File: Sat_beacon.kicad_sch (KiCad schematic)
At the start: 123 parts, among them IC1 LMX2581ESQE_NOPB, IC2 LMX2581ESQE_NOPB, J1 Conn_01x05_Pin, J2 Conn_01x05_Pin, J3 Conn_01x03_Pin, J4 MMCX, J5 MMCX, Q1 BC817-40, Q2 BC817-40, Q3 BC817-40, Q4 BC817-40, SW1 SW_SPDT_312, SW2 SW_Omron_B3FS, SW3 SW_Omron_B3FS, SW4 SW_Omron_B3FS, SW5 SW_Omron_B3FS, U1 STM32C011F6Px, U2 LD1117V33, U3 MCP1700x-330xxMB, U4 1720BL15B0050002E, U5 1720BL15B0050002E, Y1 FT2MHUPM10.0-T1

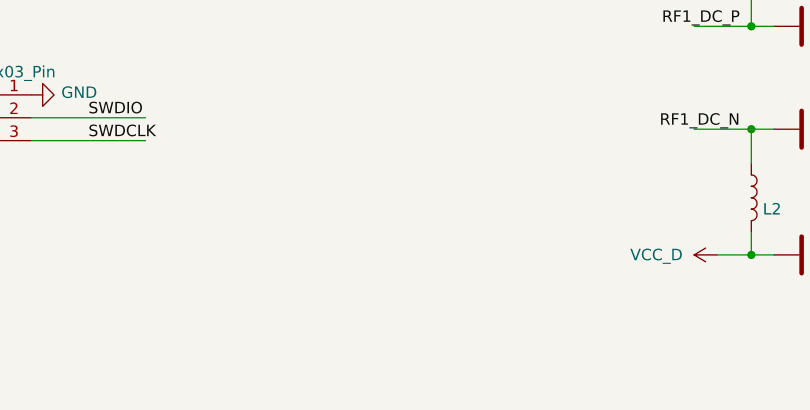
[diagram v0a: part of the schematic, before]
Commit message: RF C added, replacement needed
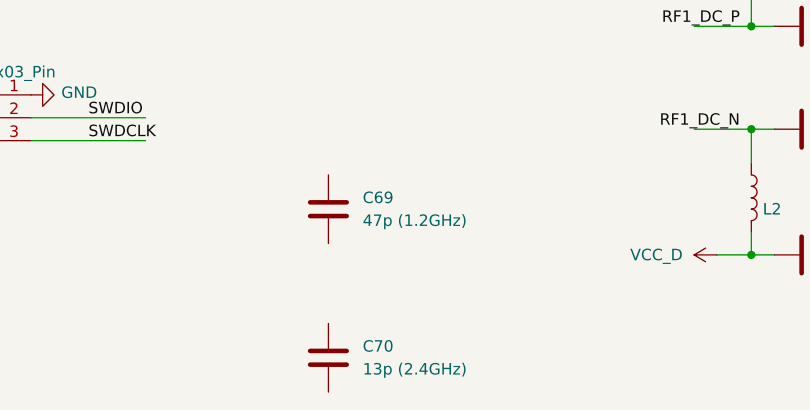
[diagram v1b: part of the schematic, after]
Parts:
- added C69: 47p (1.2GHz), Capacitor_SMD:C_0402_1005Metric, symbol Device:C
- added C70: 13p (2.4GHz), Capacitor_SMD:C_0402_1005Metric, symbol Device:C
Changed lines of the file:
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@@
+	)
+	(symbol
+		(lib_id "Device:C")
+		(at 123.19 215.9 0)
+		(unit 1)
+		(exclude_from_sim no)
+		(in_bom yes)
+		(on_board yes)
+		(dnp no)
+		(fields_autoplaced yes)
+		(property "Reference" "C70"
+			(at 127 214.6299 0)
+			(effects
+				(font
+					(size 1.27 1.27)
+				)
+				(justify left)
+			)
+		)
+		(property "Value" "13p (2.4GHz)"
+			(at 127 217.1699 0)
+			(effects
+				(font
+					(size 1.27 1.27)
+				)
+				(justify left)
+			)
+		)
+		(property "Footprint" "Capacitor_SMD:C_0402_1005Metric"
+			(at 124.1552 219.71 0)
+			(effects
+				(font
+					(size 1.27 1.27)
+				)
+				(hide yes)
+			)
+		)
+		(property "Datasheet" "https://www.tme.eu/cz/details/gjm1555c1h130gb01d/kondenzatory-mlcc-smd/murata/"
+			(at 123.19 215.9 0)
+			(effects
+				(font
+					(size 1.27 1.27)
+				)
+				(hide yes)
+			)
+		)
+		(property "Description" "Unpolarized capacitor"
+			(at 123.19 215.9 0)
+			(effects
+				(font
+					(size 1.27 1.27)
+				)
+				(hide yes)
+			)
+		)
+		(pin "2"
+		)
+		(pin "1"
+		)
+		(instances
+			(project "Sat_beacon"
+				(path "/d50b57a8-fbd1-4b9f-a519-640b54fbccac"
+					(reference "C70")
+					(unit 1)
+				)
+			)
+		)
 	)
 	(symbol
@@
 					(unit 1)
 				)
+			)
+		)
+	)
+	(symbol
+		(lib_id "Device:C")
+		(at 123.19 199.39 0)
+		(unit 1)
+		(exclude_from_sim no)
+		(in_bom yes)
+		(on_board yes)
+		(dnp no)
+		(fields_autoplaced yes)
+		(property "Reference" "C69"
+			(at 127 198.1199 0)
+			(effects
+				(font
+					(size 1.27 1.27)
+				)
+				(justify left)
+			)
+		)
+		(property "Value" "47p (1.2GHz)"
+			(at 127 200.6599 0)
+			(effects
+				(font
+					(size 1.27 1.27)
+				)
+				(justify left)
+			)
+		)
+		(property "Footprint" "Capacitor_SMD:C_0402_1005Metric"
+			(at 124.1552 203.2 0)
+			(effects
+				(font
+					(size 1.27 1.27)
+				)
+				(hide yes)
+			)
+		)
+		(property "Datasheet" "https://www.tme.eu/cz/details/gjm1555c1h470jb01d/kondenzatory-mlcc-smd/murata/"
+			(at 123.19 199.39 0)
+			(effects
+				(font
+					(size 1.27 1.27)
+				)
+				(hide yes)
+			)
+		)
+		(property "Description" "Unpolarized capacitor"
+			(at 123.19 199.39 0)
+			(effects
+				(font
+					(size 1.27 1.27)
+				)
+				(hide yes)
+			)
+		)
+		(pin "2"
+		)
+		(pin "1"
+		)
+		(instances
+			(project ""
+				(path "/d50b57a8-fbd1-4b9f-a519-640b54fbccac"
+					(reference "C69")
+					(unit 1)
+				)

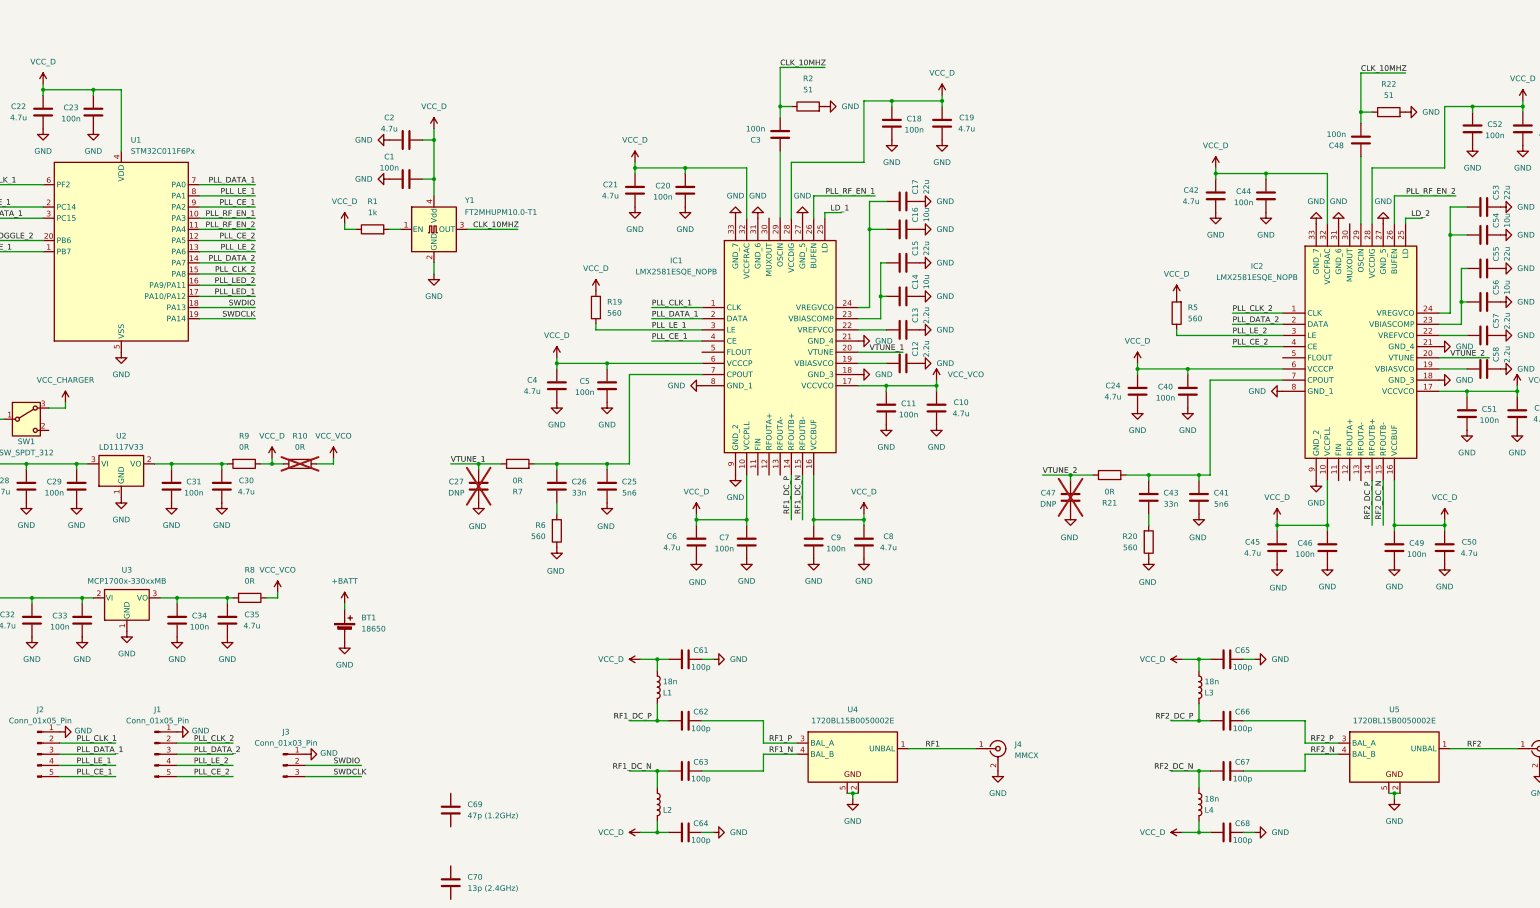
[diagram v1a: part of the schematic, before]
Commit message: footprint fixes, BOM and CSV generated
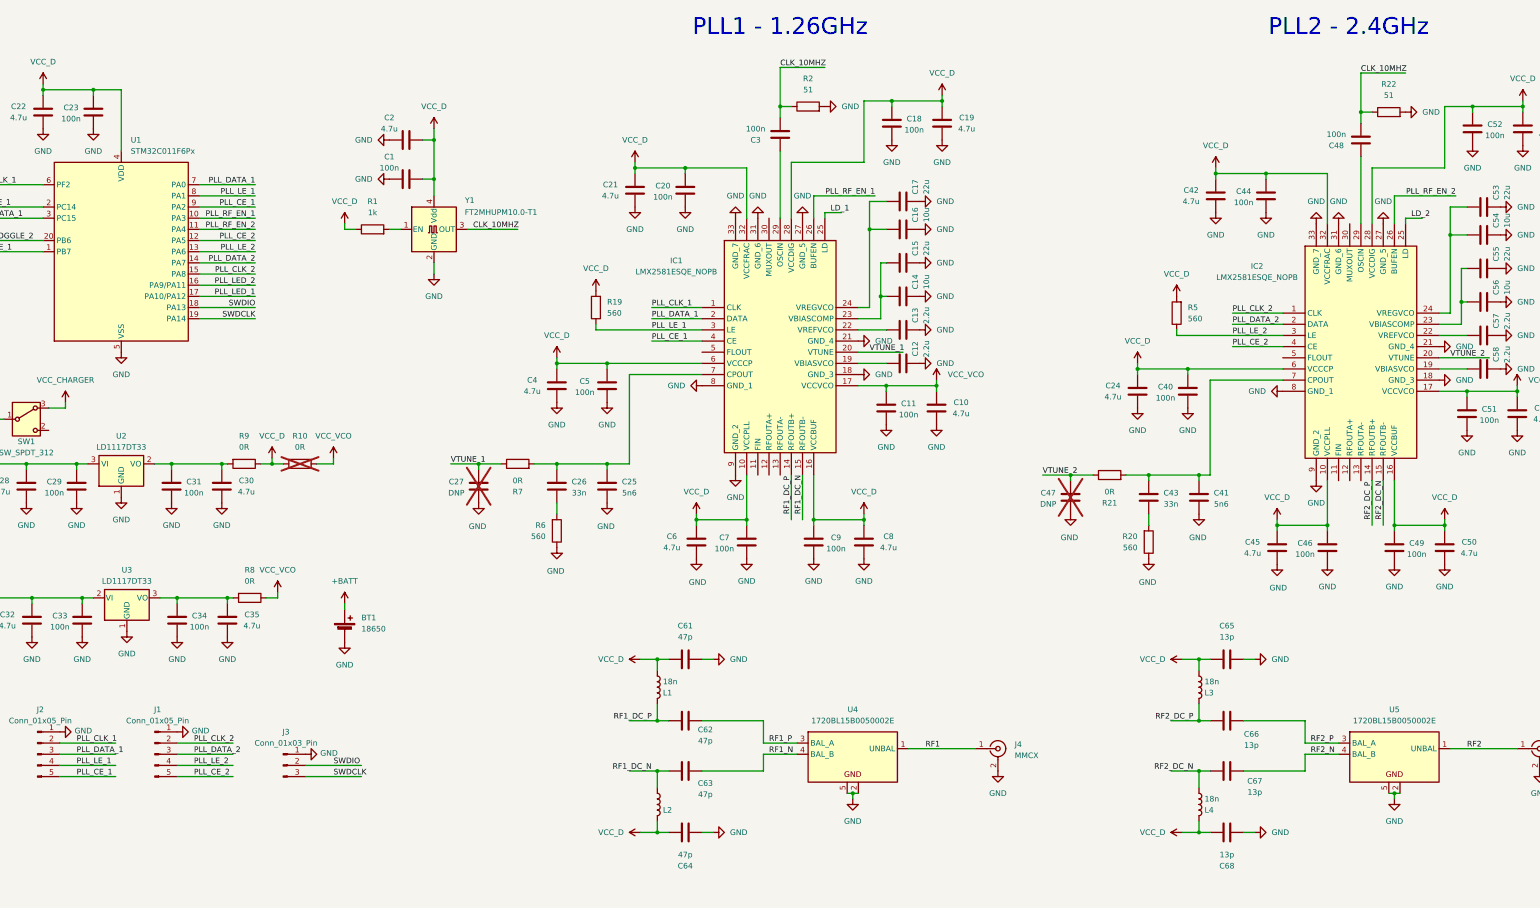
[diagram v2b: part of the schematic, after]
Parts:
- removed C69: 47p (1.2GHz), Capacitor_SMD:C_0402_1005Metric, symbol Device:C
- removed C70: 13p (2.4GHz), Capacitor_SMD:C_0402_1005Metric, symbol Device:C
- C15, C17, C53, C55: footprint Capacitor_SMD:C_0603_1608Metric -> Capacitor_SMD:C_0805_2012Metric
- C61, C62, C63, C64: value 100p -> 47p
- C65, C66, C67, C68: value 100p -> 13p
- R1, R16, R18, R23, R4: footprint Resistor_SMD:R_0805_2012Metric -> Resistor_SMD:R_0603_1608Metric
- U2: value LD1117V33 -> LD1117DT33
- U3: value MCP1700x-330xxMB -> LD1117DT33; footprint Package_TO_SOT_SMD:SOT-89-3 -> Package_TO_SOT_THT:TO-220-3_Vertical
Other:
- note added: "PLL1 - 1.26GHz"
- note added: "PLL2 - 2.4GHz"

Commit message: Separated PLL power
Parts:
- added C69, C72: 4.7u, Capacitor_SMD:C_0805_2012Metric, symbol Device:C
- added C70, C71: 100n, Capacitor_SMD:C_0603_1608Metric, symbol Device:C
- added R25, R26: 0R, Resistor_SMD:R_0603_1608Metric, symbol Device:R
- added U6: LD1117DT33, Package_TO_SOT_THT:TO-220-3_Vertical, symbol Regulator_Linear:MCP1700x-330xxMB
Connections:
- net GND: now also C69.1, C70.1, C71.1, C72.1, U6.1 (GND)
- net at C28.2, C29.2, C32.2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: now also C69.2, C70.2, U6.2 (VI)
- removed net VCC_D: C1.2, C18.2, C19.2, C2.2, C20.2, C21.2, C22.2, C23.2, C24.2, C4.2, C40.2, C42.2, C44.2, C45.2, C46.2, C49.2, C5.2, C50.2, C52.2, C6.2, C60.2, C61.1, C64.1, C65.1, C68.1, C7.2, C8.2, C9.2, D1.2 (A), D2.2 (A), D3.2 (A), D4.2 (A), IC1.10 (VCCPLL), IC1.16 (VCCBUF), IC1.28 (VCCDIG), IC1.32 (VCCFRAC), IC1.6 (VCCCP), IC2.10 (VCCPLL), IC2.16 (VCCBUF), IC2.28 (VCCDIG), IC2.32 (VCCFRAC), IC2.6 (VCCCP), L1.2, L2.1, L3.2, L4.1, R1.1, R10.2, R11.2, R12.2, R13.2, R14.2, R19.2, R5.2, R9.1, U1.4 (VDD), Y1.4 (Vdd)
- net VCC_VCO renamed VCC_PLL1
- net VCC_PLL1: now also C18.2, C19.2, C20.2, C21.2, C4.2, C5.2, C6.2, C61.1, C64.1, C7.2, C8.2, C9.2, IC1.10 (VCCPLL), IC1.16 (VCCBUF), IC1.28 (VCCDIG), IC1.32 (VCCFRAC), IC1.6 (VCCCP), L1.2, L2.1; no longer C51.2, C59.2, IC2.17 (VCCVCO), R8.1
- new net: C71.2, C72.2, R25.2, U6.3 (VO)
- new net VCC_MCU: C1.2, C2.2, C22.2, C23.2, D1.2 (A), D2.2 (A), D3.2 (A), D4.2 (A), R1.1, R10.2, R11.2, R12.2, R13.2, R14.2, R19.2, R26.2, R5.2, R9.1, U1.4 (VDD), Y1.4 (Vdd)
- new net VCC_PLL2: C24.2, C40.2, C42.2, C44.2, C45.2, C46.2, C49.2, C50.2, C51.2, C52.2, C59.2, C60.2, C65.1, C68.1, IC2.10 (VCCPLL), IC2.16 (VCCBUF), IC2.17 (VCCVCO), IC2.28 (VCCDIG), IC2.32 (VCCFRAC), IC2.6 (VCCCP), L3.2, L4.1, R26.1
- new net VCC_VPLL1: R8.1
- new net VCC_VPLL2: R25.1
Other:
- moved on the sheet: BT1, J1, J2, J3

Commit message: MMCX model added
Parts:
- J4, J5: footprint Connector_Coaxial:MMCX_Molex_73415-0961_Horizontal_0.8mm-PCB -> Library:MMCX-J-P-X-ST-EM1
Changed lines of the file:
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@@
 			)
 		)
-		(property "Footprint" "Connector_Coaxial:MMCX_Molex_73415-0961_Horizontal_0.8mm-PCB"
+		(property "Footprint" "Library:MMCX-J-P-X-ST-EM1"
 			(at 370.84 185.42 0)
 			(effects
@@
 			)
 		)
-		(property "Footprint" "Connector_Coaxial:MMCX_Molex_73415-0961_Horizontal_0.8mm-PCB"
+		(property "Footprint" "Library:MMCX-J-P-X-ST-EM1"
 			(at 247.65 185.42 0)
 			(effects

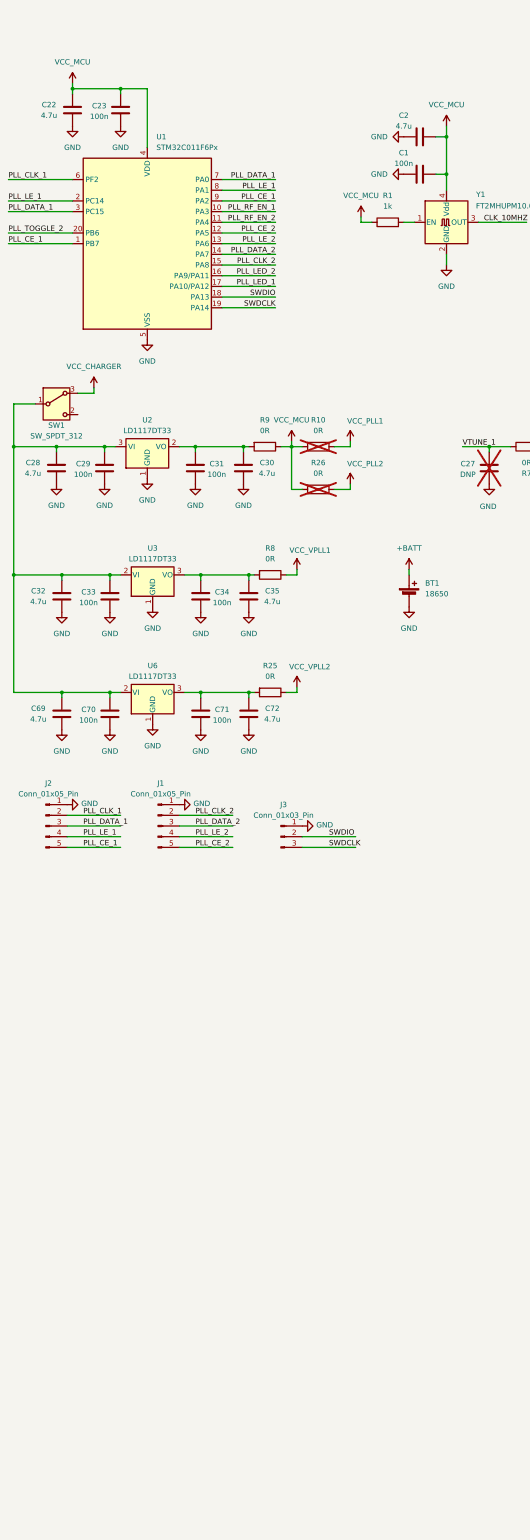
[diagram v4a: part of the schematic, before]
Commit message: MCU swap, IOC created
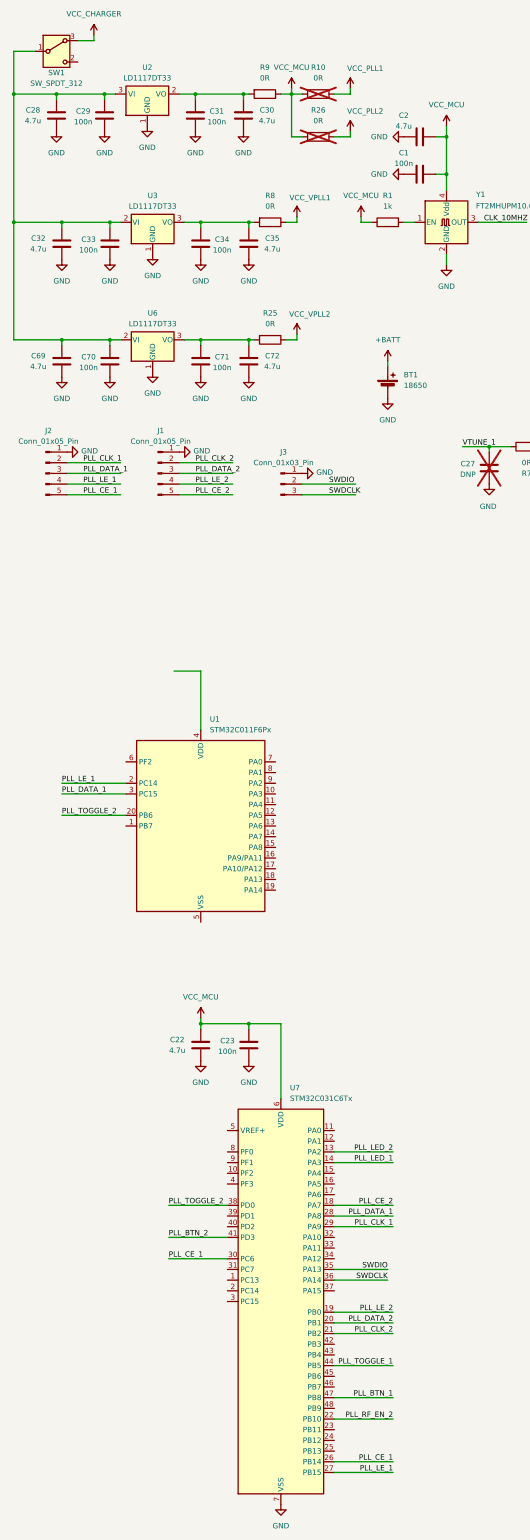
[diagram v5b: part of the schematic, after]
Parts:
- added U7: STM32C031C6Tx, Package_QFP:LQFP-48_7x7mm_P0.5mm, symbol MCU_ST_STM32C0:STM32C031C6Tx
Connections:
- net GND: now also U7.7 (VSS); no longer U1.5 (VSS)
- net PLL_BTN_1: now also U7.47 (PB8)
- net PLL_BTN_2: now also U7.41 (PD3)
- net PLL_CE_1: now also U7.26 (PB14), U7.30 (PC6); no longer U1.1 (PB7), U1.9 (PA2)
- net PLL_CE_2: now also U7.18 (PA7); no longer U1.12 (PA5)
- net PLL_CLK_1: now also U7.29 (PA9); no longer U1.6 (PF2)
- net PLL_CLK_2: now also U7.21 (PB2); no longer U1.15 (PA8)
- net PLL_DATA_1: now also U7.28 (PA8); no longer U1.7 (PA0)
- net PLL_DATA_2: now also U7.20 (PB1); no longer U1.14 (PA7)
- net PLL_LED_1: now also U7.14 (PA3); no longer U1.17 (PA10/PA12)
- net PLL_LED_2: now also U7.13 (PA2); no longer U1.16 (PA9/PA11)
- net PLL_LE_1: now also U7.27 (PB15); no longer U1.8 (PA1)
- net PLL_LE_2: now also U7.19 (PB0); no longer U1.13 (PA6)
- net PLL_RF_EN_1: no longer U1.10 (PA3)
- net PLL_RF_EN_2: now also U7.22 (PB10); no longer U1.11 (PA4)
- net PLL_TOGGLE_1: now also U7.44 (PB5)
- net PLL_TOGGLE_2: now also U7.38 (PD0)
- net SWDCLK: now also U7.36 (PA14); no longer U1.19 (PA14)
- net SWDIO: now also U7.35 (PA13); no longer U1.18 (PA13)
- net VCC_MCU: now also U7.6 (VDD); no longer U1.4 (VDD)
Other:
- moved on the sheet: BT1, C22, C23, C28, C29, C30, C31, C32, C33, C34, C35, C69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
